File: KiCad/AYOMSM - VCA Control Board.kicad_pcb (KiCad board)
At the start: 2 copper layers, 19 x 99 mm, 12 parts, among them J5 CONN_1, J6 CONN_2, SW1 LOG_LIN_SW

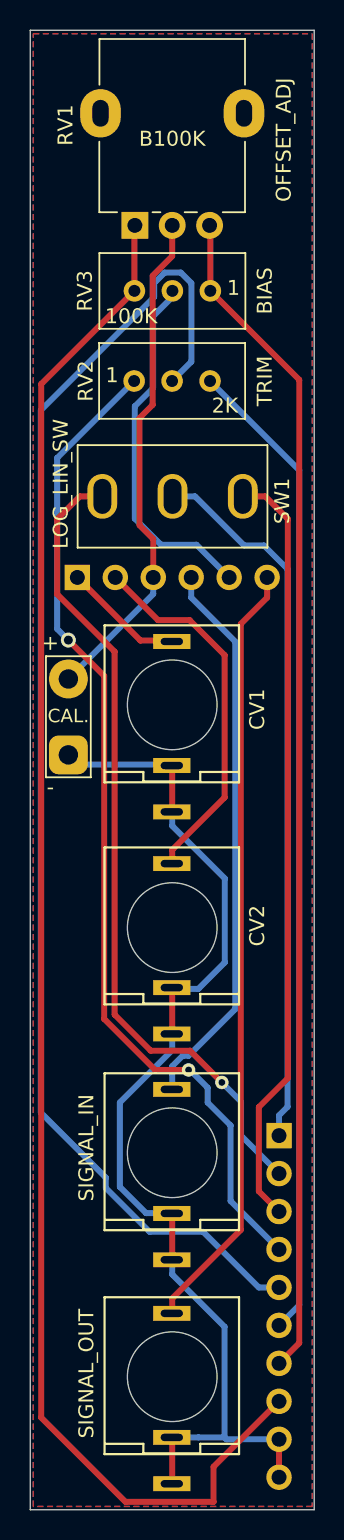
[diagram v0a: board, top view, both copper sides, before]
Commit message: Restructured repo, added Gerbers, Gerber archive, and SVG exports
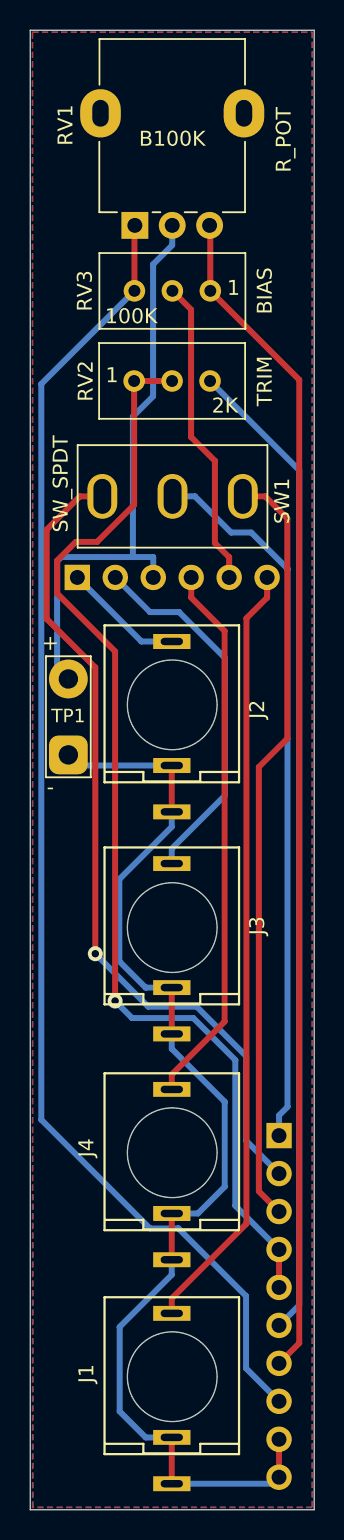
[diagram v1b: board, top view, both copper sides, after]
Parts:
- RV1: value OFFSET_ADJ -> R_POT
- SW1: value LOG_LIN_SW -> SW_SPDT
- renumbered SIGNAL_OUT to J1, CV1 to J2, CV2 to J3, SIGNAL_IN to J4, CAL. to TP1
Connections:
- J6 pad 5: /TRIM_2 -> /TRIM_1
- RV2 pad 2: /TRIM_2 -> /TRIM_1
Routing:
- net /TRIM_2: track 90.0 -> 0.00 mm
- net -12V: track 104.8 -> 89.0 mm
- net /TRIM_1: track 67.8 -> 74.7 mm, vias 2 -> 1
- net /OFFSET_ADJ: track 34.0 -> 39.4 mm
- net /BIAS: track 24.2 -> 20.8 mm
- net GND: track 74.4 -> 77.0 mm
- net /LOG_LIN_SW_2: track 55.1 -> 56.1 mm
- net /SIGNAL_IN: track 37.4 -> 36.6 mm

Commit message: Updated Gerbers and archive
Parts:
- RV1: value R_POT -> OFFSET ADJUST
- SIGNAL IN: renamed from J4
- SIGNAL OUT: renamed from J1
- SW1: value SW_SPDT -> LIN_LOG SW
- moved TP1 14.2 mm to (92.7, 102.1)
- moved RV3 14.0 mm to (88.0, 57.4)
- moved RV1 6.50 mm to (83.0, 73.6)
- moved RV2 0.38 mm to (83.0, 77.9)
- renumbered J2 to CV1, J3 to CV2
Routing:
- net +12V: track 79.2 -> 96.3 mm
- net -12V: track 89.0 -> 105.8 mm
- net /BIAS: track 20.8 -> 35.2 mm
- net /OFFSET_ADJ: track 39.4 -> 29.7 mm
- net /CV2: track 24.8 -> 20.7 mm
- net GND: track 77.0 -> 74.6 mm
- net /TRIM_1: track 74.7 -> 72.5 mm, vias 1 -> 0
- net /LOG_LIN_SW_1: track 47.9 -> 50.0 mm
- net /LOG_LIN_SW_2: track 56.1 -> 54.5 mm, vias 1 -> 0
- net /CV1: track 8.10 -> 8.77 mm
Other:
- net class Default: clearance 0.3 -> 0.25; trace_width 0.4 -> 0.3
- rule trace_clearance: 0.3 -> 0.25
- board text added: "Shapetaker Audio - Utility VCA Control Board (Rev 1.2)"
- board text removed: "Shapetaker Audio - Utility VCA Control Board (Rev 1.0)"

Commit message: Updated Gerbers
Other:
- board text added: "Shapetaker Audio - Utility VCA Control Board (Rev 1.3)"
- board text removed: "Original Design by Ray Wilson (Music From Outer Space)"
- board text removed: "Shapetaker Audio - Utility VCA Control Board (Rev 1.2)"
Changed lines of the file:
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@@
   (general
     (thickness 1.6)
-    (drawings 15)
+    (drawings 14)
     (tracks 121)
     (zones 0)
@@
     (arrow2b (pts (xy 76 51.816) (xy 77.126504 51.229579)))
   )
-  (gr_text "Original Design by Ray Wilson (Music From Outer Space)" (at 77.343 130.683 90) (layer B.SilkS)
+  (gr_text "Shapetaker Audio - Utility VCA Control Board (Rev 1.3)" (at 77.414 131.083 90) (layer B.SilkS)
     (effects (font (size 1 1) (thickness 0.15)) (justify mirror))
   )
-  (gr_text "Shapetaker Audio - Utility VCA Control Board (Rev 1.2)" (at 93.853 98.171 90) (layer B.SilkS)
-    (effects (font (size 1 1) (thickness 0.15)) (justify mirror))
-  )
